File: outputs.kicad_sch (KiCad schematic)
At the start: 36 parts, among them J4 PH-2P, J5 PH-2P, J6 PH-3P, J7 MF3-2P, J8 PH-3P, J9 XH-4P, Q1 AON7804, Q2 AON7524, U5 74LVC2G17, U6 TMC2209-LA

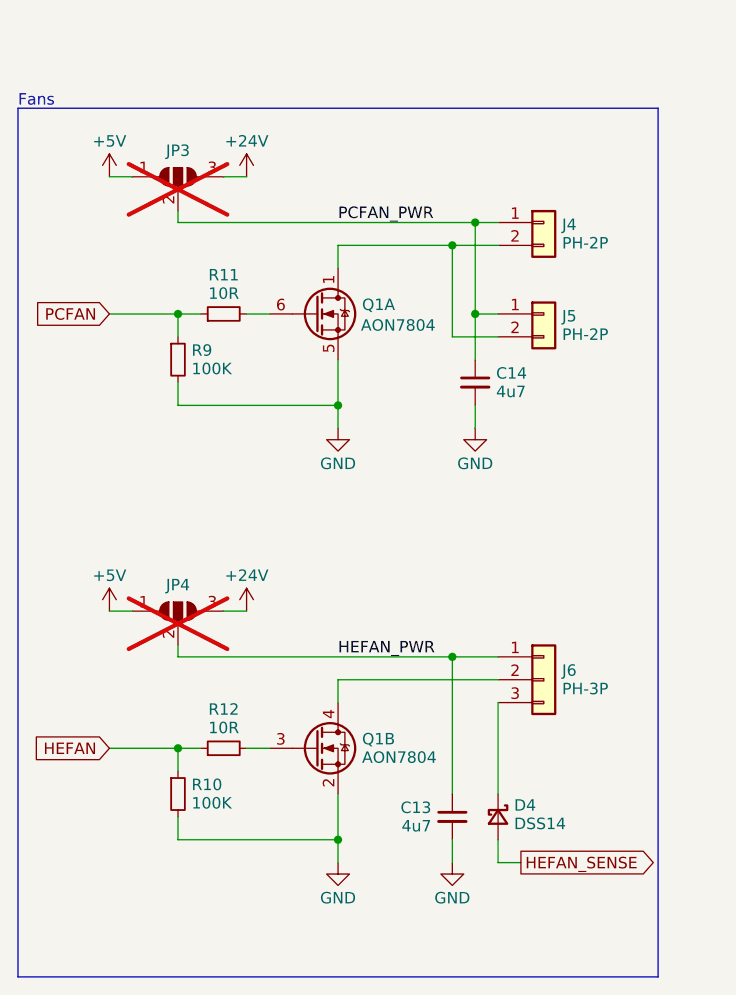
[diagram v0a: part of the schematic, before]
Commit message: Remove DNP from stuff where it doesn't belong in the schematic. Also DNP the fan port caps (the BOM ones weren't rated good for 24V anyway), but in any case since I couldn't find 4.7uF/35V/0603 good for 105C, reduce them to 2.2uF. Too bad I didn't make them 0805
Also added note for higher temp STM32, so I think all the components
should be good to 105C, except for the JST connectors...
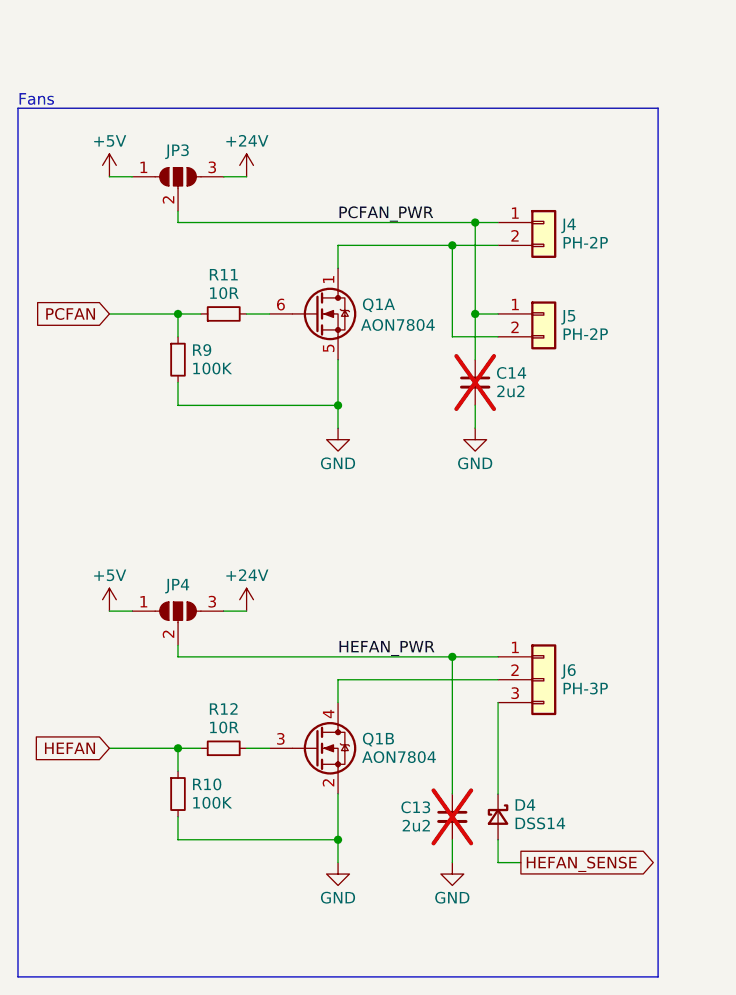
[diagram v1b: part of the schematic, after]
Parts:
- C13, C14: value 4u7 -> 2u2; LCSC C19666 -> C408135; Notes (none) -> 35V X6S; manf# CL10A475KO8NNNC -> GRM188C8YA225KE11D; now not fitted
- C16, C18, C19, C20, C21: Notes (none) -> 50V
- JP3, JP4: now fitted

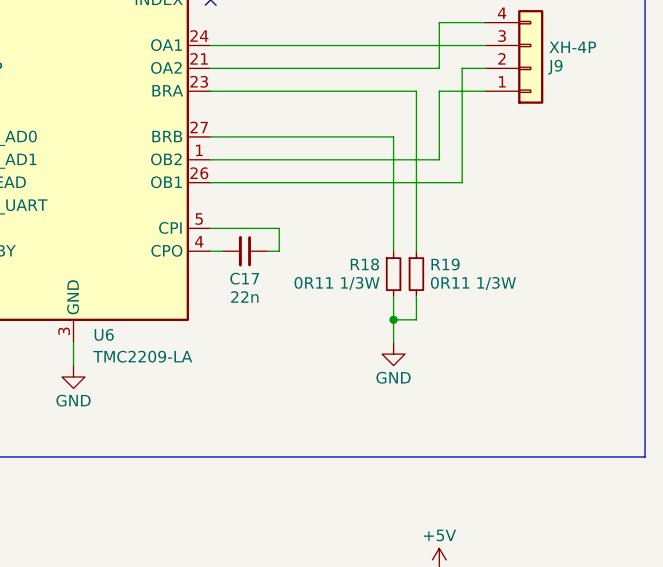
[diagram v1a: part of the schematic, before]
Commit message: Fix LCSC part for 74LVC2G17 (wrong package). List alternate parts in notes fields.
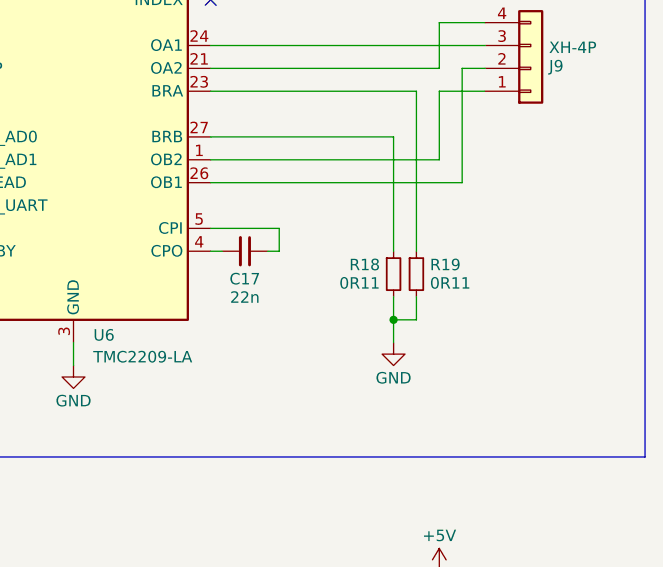
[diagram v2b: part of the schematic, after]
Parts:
- R18, R19: value 0R11 1/3W -> 0R11; Notes (none) -> 1/3 W
- U5: LCSC C7394037 -> C7394022
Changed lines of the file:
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@@
 			)
 		)
-		(property "Value" "0R11 1/3W"
+		(property "Value" "0R11"
 			(at 227.5586 82.304 0)
 			(effects
@@
 			)
 		)
-		(property "Notes" ""
+		(property "Notes" "1/3 W"
 			(at 226.06 81.28 0)
 			(effects
@@
 			)
 		)
-		(property "Datasheet" "~"
+		(property "Datasheet" "https://www.smc-diodes.com/propdf/DSS12U%20THRU%20DSS125U%20N1873%20REV.A.pdf"
 			(at 78.74 172.72 90)
 			(effects
@@
 			)
 		)
-		(property "LCSC" "C7394037"
+		(property "LCSC" "C7394022"
 			(at 58.42 45.72 0)
 			(effects
@@
 			)
 		)
-		(property "LCSC" "C7394037"
+		(property "LCSC" "C7394022"
 			(at 228.6 127 0)
 			(effects
@@
 			)
 		)
-		(property "Value" "0R11 1/3W"
+		(property "Value" "0R11"
 			(at 222.0214 82.304 0)
 			(effects
@@
 			)
 		)
-		(property "Notes" ""
+		(property "Notes" "1/3 W"
 			(at 223.52 81.28 0)
 			(effects
@@
 			)
 		)
-		(property "LCSC" "C7394037"
+		(property "LCSC" "C7394022"
 			(at 142.24 129.54 0)
 			(effects
